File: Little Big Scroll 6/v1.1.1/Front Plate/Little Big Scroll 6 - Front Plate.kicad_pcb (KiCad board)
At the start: 2 copper layers, 59.2 x 87 mm, 15 parts, among them SW1 SW_MX_HS, SW2 SW_MX_HS, SW3 SW_MX_HS, SW4 SW_MX_HS, SW5 SW_MX_HS, SW6 SW_MX_HS

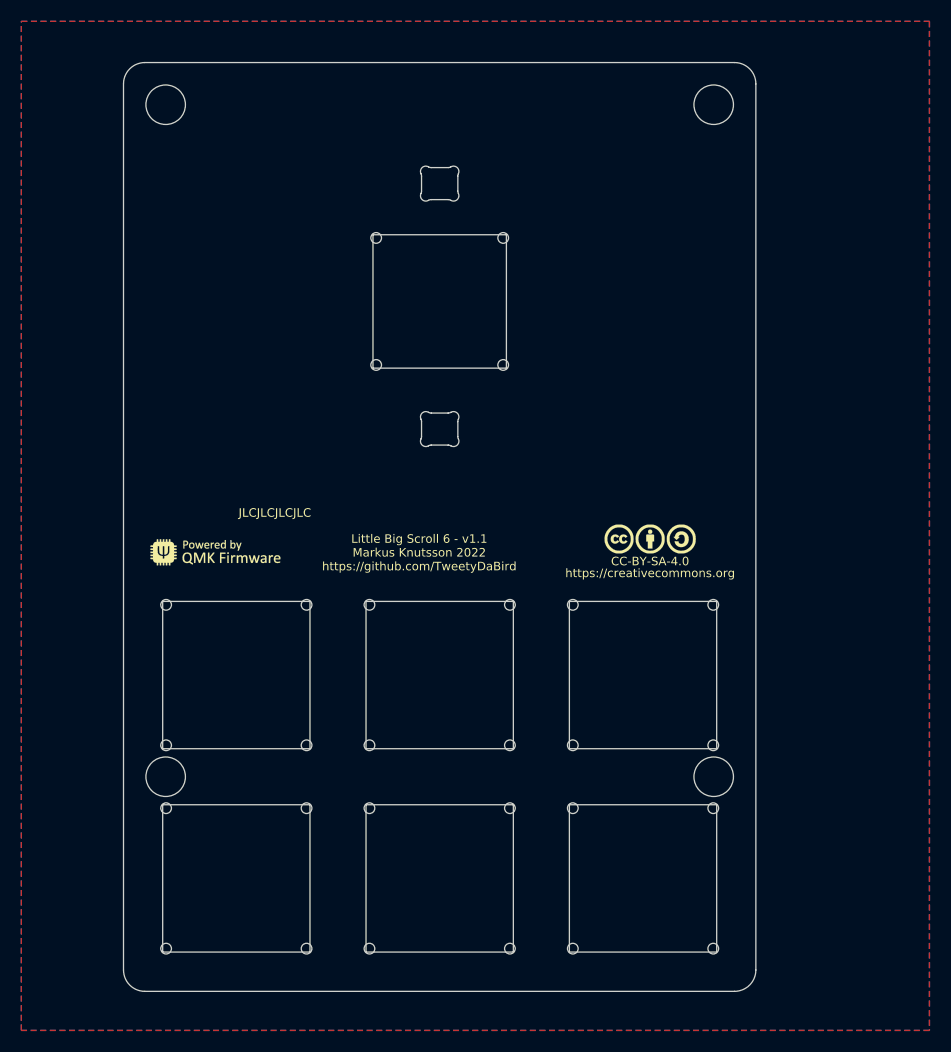
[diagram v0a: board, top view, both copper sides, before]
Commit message: LBS6 v1.1.1
Fixed plate holes
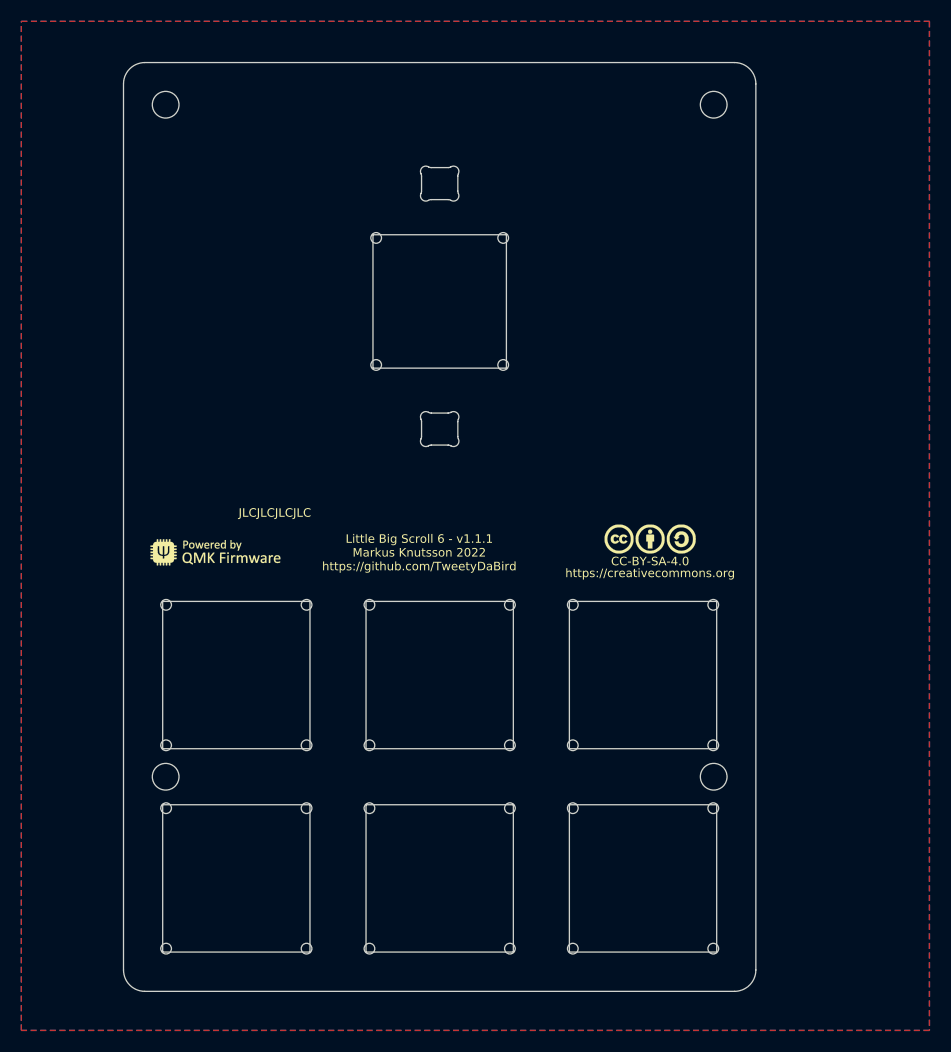
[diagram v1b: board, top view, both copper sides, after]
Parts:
- H1, H2, H3, H4: footprint Keyboard Switches & Encoders:Spacer PCB hole -> Keyboard_Plate:Spacer Plate hole
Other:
- board text added: "Little Big Scroll 6 - v1.1.1 Markus Knutsson 2022 https://github.com/TweetyDaBird"
- board text removed: "Little Big Scroll 6 - v1.1 Markus Knutsson 2022 https://github.com/TweetyDaBird"
